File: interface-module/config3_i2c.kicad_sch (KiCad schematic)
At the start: 11 parts, among them U301 TCA9548

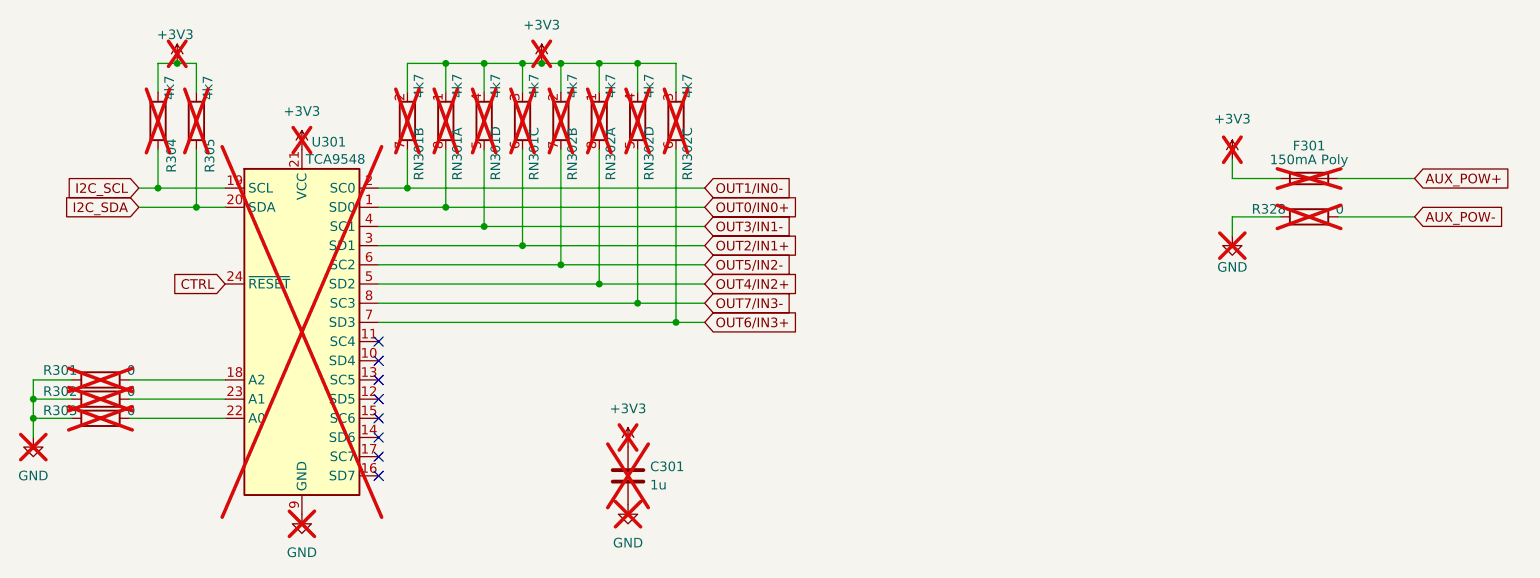
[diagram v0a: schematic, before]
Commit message: remove dnp attributes for different variants
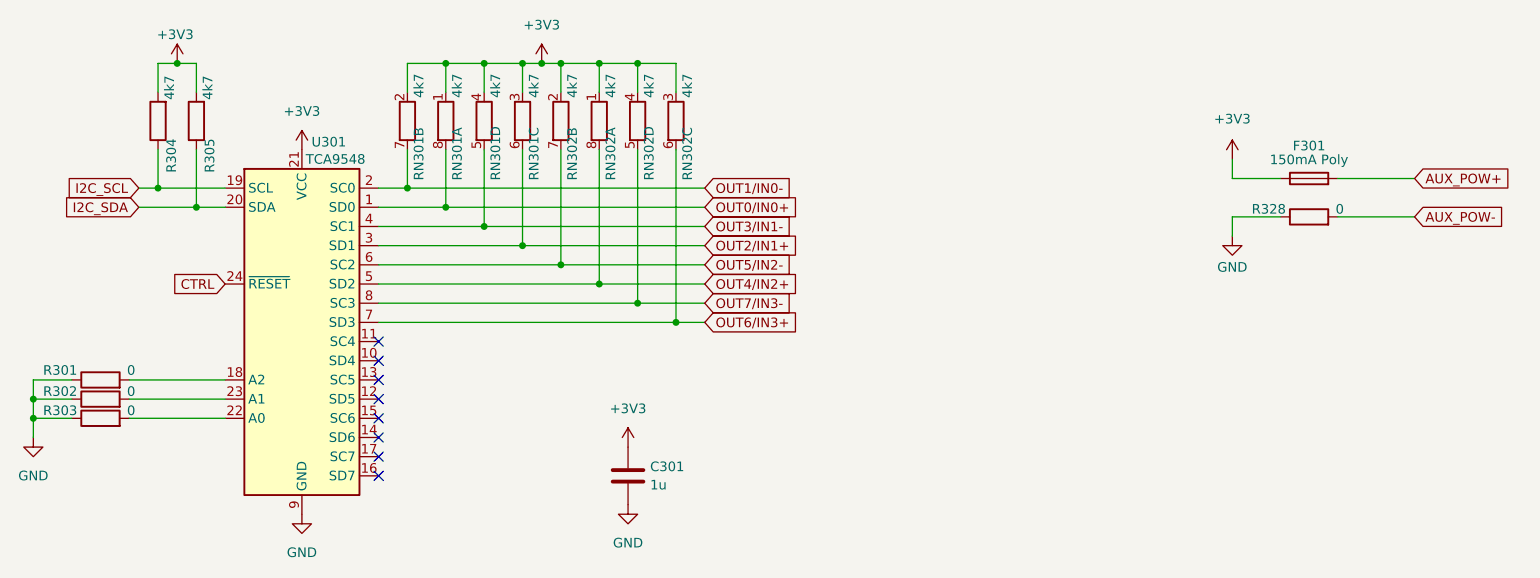
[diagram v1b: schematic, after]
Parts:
- C301, F301, R301, R302, R303, R304, R305, R328, RN301, RN302, U301: now fitted
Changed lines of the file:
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@@
 		(in_bom yes)
 		(on_board yes)
-		(dnp yes)
+		(dnp no)
 		(property "Reference" "RN301"
 			(at 205.994 113.284 90)
@@
 		(in_bom yes)
 		(on_board yes)
-		(dnp yes)
+		(dnp no)
 		(property "Reference" "R305"
 			(at 178.308 112.268 90)
@@
 		(in_bom yes)
 		(on_board yes)
-		(dnp yes)
+		(dnp no)
 		(property "Reference" "RN302"
 			(at 226.314 113.284 90)
@@
 		(in_bom yes)
 		(on_board yes)
-		(dnp yes)
+		(dnp no)
 		(fields_autoplaced yes)
 		(property "Reference" "#PWR0103"
@@
 		(in_bom yes)
 		(on_board yes)
-		(dnp yes)
+		(dnp no)
 		(property "Reference" "R302"
 			(at 158.496 141.224 90)
@@
 		(in_bom yes)
 		(on_board yes)
-		(dnp yes)
+		(dnp no)
 		(property "Reference" "R301"
 			(at 158.496 138.43 90)
@@
 		(in_bom yes)
 		(on_board yes)
-		(dnp yes)
+		(dnp no)
 		(fields_autoplaced yes)
 		(property "Reference" "#PWR0403"
@@
 		(in_bom yes)
 		(on_board yes)
-		(dnp yes)
+		(dnp no)
 		(property "Reference" "RN302"
 			(at 231.394 113.284 90)
@@
 		(in_bom yes)
 		(on_board yes)
-		(dnp yes)
+		(dnp no)
 		(property "Reference" "RN301"
 			(at 216.154 113.284 90)
@@
 		(in_bom yes)
 		(on_board yes)
-		(dnp yes)
+		(dnp no)
 		(property "Reference" "U301"
 			(at 191.77 108.204 0)
@@
 		(in_bom yes)
 		(on_board yes)
-		(dnp yes)
+		(dnp no)
 		(property "Reference" "RN301"
 			(at 211.074 113.284 90)
@@
 		(in_bom yes)
 		(on_board yes)
-		(dnp yes)
+		(dnp no)
 		(fields_autoplaced yes)
 		(property "Reference" "C301"
@@
 		(in_bom yes)
 		(on_board yes)
-		(dnp yes)
+		(dnp no)
 		(fields_autoplaced yes)
 		(property "Reference" "#PWR0401"
@@
 		(in_bom yes)
 		(on_board yes)
-		(dnp yes)
+		(dnp no)
 		(property "Reference" "R328"
 			(at 318.516 117.094 90)
@@
 		(in_bom yes)
 		(on_board yes)
-		(dnp yes)
+		(dnp no)
 		(property "Reference" "F301"
 			(at 323.85 108.712 90)
@@
 		(in_bom yes)
 		(on_board yes)
-		(dnp yes)
+		(dnp no)
 		(property "Reference" "RN302"
 			(at 236.474 113.284 90)
@@
 		(in_bom yes)
 		(on_board yes)
-		(dnp yes)
+		(dnp no)
 		(property "Reference" "R303"
 			(at 158.496 143.764 90)
@@
 		(in_bom yes)
 		(on_board yes)
-		(dnp yes)
+		(dnp no)
 		(fields_autoplaced yes)
 		(property "Reference" "#PWR0406"
@@
 		(in_bom yes)
 		(on_board yes)
-		(dnp yes)
+		(dnp no)
 		(property "Reference" "RN302"
 			(at 241.554 113.284 90)
@@
 		(in_bom yes)
 		(on_board yes)
-		(dnp yes)
+		(dnp no)
 		(property "Reference" "RN301"
 			(at 221.234 113.284 90)
@@
 		(in_bom yes)
 		(on_board yes)
-		(dnp yes)
+		(dnp no)
 		(fields_autoplaced yes)
 		(property "Reference" "#PWR0407"
@@
 		(in_bom yes)
 		(on_board yes)
-		(dnp yes)
+		(dnp no)
 		(fields_autoplaced yes)
 		(property "Reference" "#PWR0404"
@@
 		(in_bom yes)
 		(on_board yes)
-		(dnp yes)
+		(dnp no)
 		(property "Reference" "#PWR0102"
 			(at 313.69 114.3 0)
@@
 		(in_bom yes)
 		(on_board yes)
-		(dnp yes)
+		(dnp no)
 		(property "Reference" "R304"
 			(at 173.228 112.268 90)
@@
 		(in_bom yes)
 		(on_board yes)
-		(dnp yes)
+		(dnp no)
 		(fields_autoplaced yes)
 		(property "Reference" "#PWR0405"
@@
 		(in_bom yes)
 		(on_board yes)
-		(dnp yes)
+		(dnp no)
 		(property "Reference" "#PWR0402"
 			(at 173.99 101.6 0)
